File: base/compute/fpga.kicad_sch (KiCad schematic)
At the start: 17 parts, among them U4 W25X20CLSN, U5 ICE40UP5K-SG48ITR-FPGA_Lattice

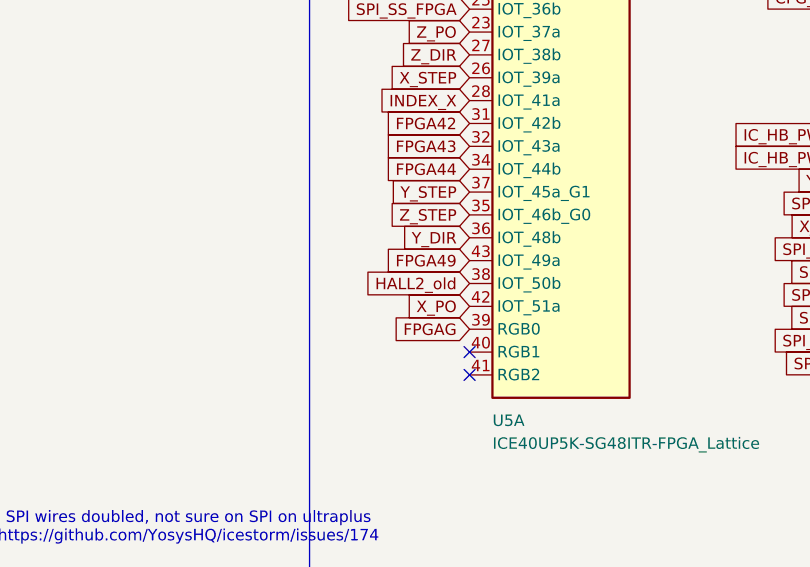
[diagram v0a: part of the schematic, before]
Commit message: kicost integration for compute and extension
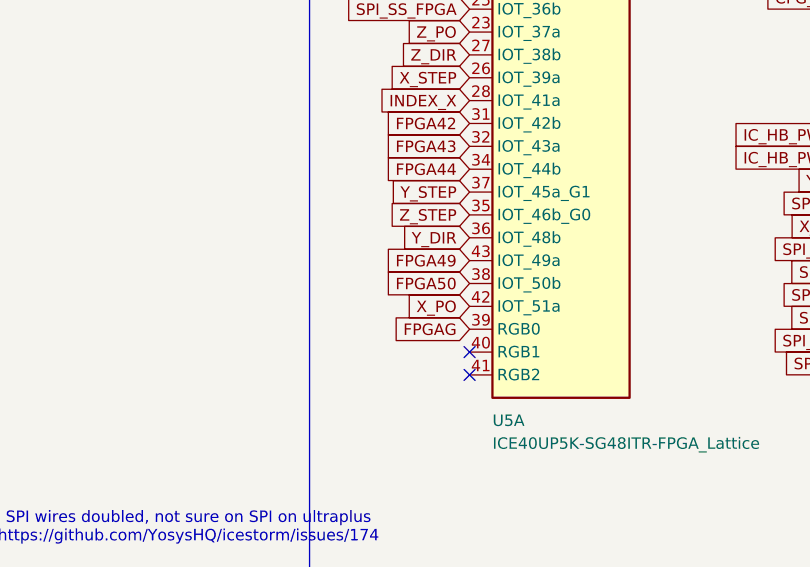
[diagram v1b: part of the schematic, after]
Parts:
- C12, C14, C3, C5, C6: Farnell 1414663 -> (none); Mouser 80-C0805C104J5R -> (none); Producer C0805C104J5RACTU -> (none); farnell# (none) -> 1414663; manf# (none) -> C0805C104J5RACTU; mouser# (none) -> 80-C0805C104J5R
- C13, C4, C7, C8: Farnell 2611942 -> (none); Mouser 81-GRM21BR61H475KE1L -> (none); Producer GRM21BR61H475KE51L -> (none); farnell# (none) -> 2611942; manf# (none) -> GRM21BR61H475KE51L; mouser# (none) -> 81-GRM21BR61H475KE1L
- D1: Farnell 1843668 -> (none); Mouser 621-B340A-F -> (none); Producer B340A-13-F -> (none); farnell# (none) -> 2393466; manf# (none) -> SD103AWS-E3-08; mouser# (none) -> 78-SD103AWS-HE3-18
- R1, R2, R3, R7: Farnell 2826162 -> (none); Mouser 71-CRCW080510K0JNEAC -> (none); Producer CRCW080510K0JNEAC -> (none); farnell# (none) -> 2826162; manf# (none) -> CRCW080510K0JNEAC; mouser# (none) -> 71-CRCW080510K0JNEAC
- R10: Farnell 1652906 -> (none); Mouser 71-CRCW0805-100 -> (none); Producer CRCW0805100RFKTA -> (none); farnell# (none) -> 1652906; manf# (none) -> CRCW0805100RFKTA; mouser# (none) -> 71-CRCW0805-100
- U4: Mouser 454-W25X20CLSNIG -> (none); Producer W25X20CLSNIG -> (none); manf# (none) -> W25X20CLSNIG; mouser# (none) -> 454-W25X20CLSNIG
- U5: Mouser 842-ICE40UP5K-SG48I -> (none); Producer ICE40UP5K-SG48I -> (none); manf# (none) -> ICE40UP5K-SG48I; mouser# (none) -> 842-ICE40UP5K-SG48I
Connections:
- net HALL2_old renamed FPGA50
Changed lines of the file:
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@@
 	(title_block
 		(title "Firestarter ")
-		(date "2024-07-25")
+		(date "2024-10-26")
 		(company "Hexastorm")
 		(comment 1 "v1")
@@
 		)
 	)
-	(global_label "HALL2_old"
+	(global_label "FPGA50"
 		(shape input)
 		(at 73.66 80.01 180)
@@
 			)
 		)
-		(property "Producer" "ICE40UP5K-SG48I"
+		(property "manf#" "ICE40UP5K-SG48I"
 			(at 199.39 58.42 0)
 			(effects
@@
 			)
 		)
-		(property "Mouser" "842-ICE40UP5K-SG48I"
+		(property "mouser#" "842-ICE40UP5K-SG48I"
 			(at 199.39 58.42 0)
 			(effects
@@
 			)
 		)
-		(property "Farnell" "2826162"
+		(property "farnell#" "2826162"
 			(at 158.75 57.15 0)
 			(effects
@@
 			)
 		)
-		(property "Producer" "CRCW080510K0JNEAC "
+		(property "manf#" "CRCW080510K0JNEAC"
 			(at 158.75 57.15 0)
 			(effects
@@
 			)
 		)
-		(property "Mouser" "71-CRCW080510K0JNEAC "
+		(property "mouser#" "71-CRCW080510K0JNEAC"
 			(at 158.75 57.15 0)
 			(effects
@@
 			)
 		)
-		(property "Farnell" "2826162"
+		(property "farnell#" "2826162"
 			(at 158.75 62.23 0)
 			(effects
@@
 			)
 		)
-		(property "Producer" "CRCW080510K0JNEAC "
+		(property "manf#" "CRCW080510K0JNEAC"
 			(at 158.75 62.23 0)
 			(effects
@@
 			)
 		)
-		(property "Mouser" "71-CRCW080510K0JNEAC "
+		(property "mouser#" "71-CRCW080510K0JNEAC"
 			(at 158.75 62.23 0)
 			(effects
@@
 			)
 		)
-		(property "Producer" "B340A-13-F"
+		(property "manf#" "SD103AWS-E3-08"
 			(at 175.26 109.22 0)
 			(effects
@@
 			)
 		)
-		(property "Farnell" "1843668 "
+		(property "farnell#" "2393466"
 			(at 175.26 109.22 0)
 			(effects
@@
 			)
 		)
-		(property "Mouser" "621-B340A-F"
+		(property "mouser#" "78-SD103AWS-HE3-18"
 			(at 175.26 109.22 0)
 			(effects
@@
 			)
 		)
-		(property "Producer" "ICE40UP5K-SG48I"
+		(property "manf#" "ICE40UP5K-SG48I"
 			(at 198.12 105.41 0)
 			(effects
@@
 			)
 		)
-		(property "Mouser" "842-ICE40UP5K-SG48I"
+		(property "mouser#" "842-ICE40UP5K-SG48I"
 			(at 198.12 105.41 0)
 			(effects
@@
 			)
 		)
-		(property "Mouser" "454-W25X20CLSNIG"
+		(property "mouser#" "454-W25X20CLSNIG"
 			(at 111.76 149.86 0)
 			(effects
@@
 			)
 		)
-		(property "Producer" "W25X20CLSNIG "
+		(property "manf#" "W25X20CLSNIG"
 			(at 111.76 149.86 0)
 			(effects
@@
 		)
 		(instances
-			(project ""
+			(project "main_board"
 				(path "/3f5fe6b7-98fc-4d3e-9567-f9f7202d1455/bdb11667-3ffd-4676-bd47-34e666a8a2df"
 					(reference "U4")
@@
 			)
 		)
-		(property "Producer" "C0805C104J5RACTU"
+		(property "manf#" "C0805C104J5RACTU"
 			(at 114.3 137.16 0)
 			(effects
@@
 			)
 		)
-		(property "Mouser" "80-C0805C104J5R "
+		(property "mouser#" "80-C0805C104J5R"
 			(at 114.3 137.16 0)
 			(effects
@@
 			)
 		)
-		(property "Farnell" "1414663 "
+		(property "farnell#" "1414663"
 			(at 114.3 137.16 0)
 			(effects
@@
 			)
 		)
-		(property "Producer" "C0805C104J5RACTU"
+		(property "manf#" "C0805C104J5RACTU"
 			(at 210.82 39.37 0)
 			(effects
@@
 			)
 		)
-		(property "Mouser" "80-C0805C104J5R "
+		(property "mouser#" "80-C0805C104J5R"
 			(at 210.82 39.37 0)
 			(effects
@@
 			)
 		)
-		(property "Farnell" "1414663 "
+		(property "farnell#" "1414663"
 			(at 210.82 39.37 0)
 			(effects
@@
 			)
 		)
-		(property "Producer" "GRM21BR61H475KE51L"
+		(property "manf#" "GRM21BR61H475KE51L"
 			(at 105.41 38.1 0)
 			(effects
@@
 			)
 		)
-		(property "Farnell" "2611942"
+		(property "farnell#" "2611942"
 			(at 105.41 38.1 0)
 			(effects
@@
 			)
 		)
-		(property "Mouser" "81-GRM21BR61H475KE1L"
+		(property "mouser#" "81-GRM21BR61H475KE1L"
 			(at 105.41 38.1 0)
 			(effects
@@
 			)
 		)
-		(property "Producer" "GRM21BR61H475KE51L"
+		(property "manf#" "GRM21BR61H475KE51L"
 			(at 151.13 36.83 0)
 			(effects
@@
 			)
 		)
-		(property "Farnell" "2611942"
+		(property "farnell#" "2611942"
 			(at 151.13 36.83 0)
 			(effects
@@
 			)
 		)
-		(property "Mouser" "81-GRM21BR61H475KE1L"
+		(property "mouser#" "81-GRM21BR61H475KE1L"
 			(at 151.13 36.83 0)
 			(effects
@@
 			)
 		)
-		(property "Producer" "ICE40UP5K-SG48I"
+		(property "manf#" "ICE40UP5K-SG48I"
 			(at 83.82 64.77 0)
 			(effects
@@
 			)
 		)
-		(property "Mouser" "842-ICE40UP5K-SG48I"
+		(property "mouser#" "842-ICE40UP5K-SG48I"
 			(at 83.82 64.77 0)
 			(effects
@@
 			)
 		)
-		(property "Producer" "GRM21BR61H475KE51L"
+		(property "manf#" "GRM21BR61H475KE51L"
 			(at 185.42 100.33 0)
 			(effects
@@
 			)
 		)
-		(property "Farnell" "2611942"
+		(property "farnell#" "2611942"
 			(at 185.42 100.33 0)
 			(effects
@@
 			)
 		)
-		(property "Mouser" "81-GRM21BR61H475KE1L"
+		(property "mouser#" "81-GRM21BR61H475KE1L"
 			(at 185.42 100.33 0)
 			(effects
@@
 			)
 		)
-		(property "Producer" "C0805C104J5RACTU"
+		(property "manf#" "C0805C104J5RACTU"
 			(at 95.25 38.1 0)
 			(effects
@@
 			)
 		)
-		(property "Mouser" "80-C0805C104J5R "
+		(property "mouser#" "80-C0805C104J5R"
 			(at 95.25 38.1 0)
 			(effects
@@
 			)
 		)
-		(property "Farnell" "1414663 "
+		(property "farnell#" "1414663"
 			(at 95.25 38.1 0)
 			(effects
@@
 			)
 		)
-		(property "Farnell" "2826162"
+		(property "farnell#" "2826162"
 			(at 82.55 138.43 0)
 			(effects
@@
 			)
 		)
-		(property "Producer" "CRCW080510K0JNEAC "
+		(property "manf#" "CRCW080510K0JNEAC"
 			(at 82.55 138.43 0)
 			(effects
@@
 			)
 		)
-		(property "Mouser" "71-CRCW080510K0JNEAC "
+		(property "mouser#" "71-CRCW080510K0JNEAC"
 			(at 82.55 138.43 0)
 			(effects
@@
 			)
 		)
-		(property "Producer" "C0805C104J5RACTU"
+		(property "manf#" "C0805C104J5RACTU"
 			(at 143.51 36.83 0)
 			(effects
@@
 			)
 		)
-		(property "Mouser" "80-C0805C104J5R "
+		(property "mouser#" "80-C0805C104J5R"
 			(at 143.51 36.83 0)
 			(effects
@@
 			)
 		)
-		(property "Farnell" "1414663 "
+		(property "farnell#" "1414663"
 			(at 143.51 36.83 0)
 			(effects
@@
 			)
 		)
-		(property "Producer" "GRM21BR61H475KE51L"
+		(property "manf#" "GRM21BR61H475KE51L"
 			(at 217.17 39.37 0)
 			(effects
@@
 			)
 		)
-		(property "Farnell" "2611942"
+		(property "farnell#" "2611942"
 			(at 217.17 39.37 0)
 			(effects
@@
 			)
 		)
-		(property "Mouser" "81-GRM21BR61H475KE1L"
+		(property "mouser#" "81-GRM21BR61H475KE1L"
 			(at 217.17 39.37 0)
 			(effects
@@
 			)
 		)
-		(property "Producer" "CRCW0805100RFKTA"
+		(property "manf#" "CRCW0805100RFKTA"
 			(at 175.26 102.87 90)
 			(effects
@@
 			)
 		)
-		(property "Mouser" "71-CRCW0805-100"
+		(property "mouser#" "71-CRCW0805-100"
 			(at 175.26 102.87 90)
 			(effects
@@
 			)
 		)
-		(property "Farnell" "1652906"
+		(property "farnell#" "1652906"
 			(at 175.26 102.87 90)
 			(effects
@@
 			)
 		)
-		(property "Producer" "C0805C104J5RACTU"
+		(property "manf#" "C0805C104J5RACTU"
 			(at 179.07 100.33 0)
 			(effects
@@
 			)
 		)
-		(property "Mouser" "80-C0805C104J5R "
+		(property "mouser#" "80-C0805C104J5R"
 			(at 179.07 100.33 0)
 			(effects
@@
 			)
 		)
-		(property "Farnell" "1414663 "
+		(property "farnell#" "1414663"
 			(at 179.07 100.33 0)
 			(effects
@@
 			)
 		)
-		(property "Producer" "ICE40UP5K-SG48I"
+		(property "manf#" "ICE40UP5K-SG48I"
 			(at 129.54 66.04 0)
 			(effects
@@
 			)
 		)
-		(property "Mouser" "842-ICE40UP5K-SG48I"
+		(property "mouser#" "842-ICE40UP5K-SG48I"
 			(at 129.54 66.04 0)
 			(effects
@@
 			)
 		)
-		(property "Farnell" "2826162"
+		(property "farnell#" "2826162"
 			(at 78.74 138.43 0)
 			(effects
@@
 			)
 		)
-		(property "Producer" "CRCW080510K0JNEAC "
+		(property "manf#" "CRCW080510K0JNEAC"
 			(at 78.74 138.43 0)
 			(effects
@@
 			)
 		)
-		(property "Mouser" "71-CRCW080510K0JNEAC "
+		(property "mouser#" "71-CRCW080510K0JNEAC"
 			(at 78.74 138.43 0)
 			(effects

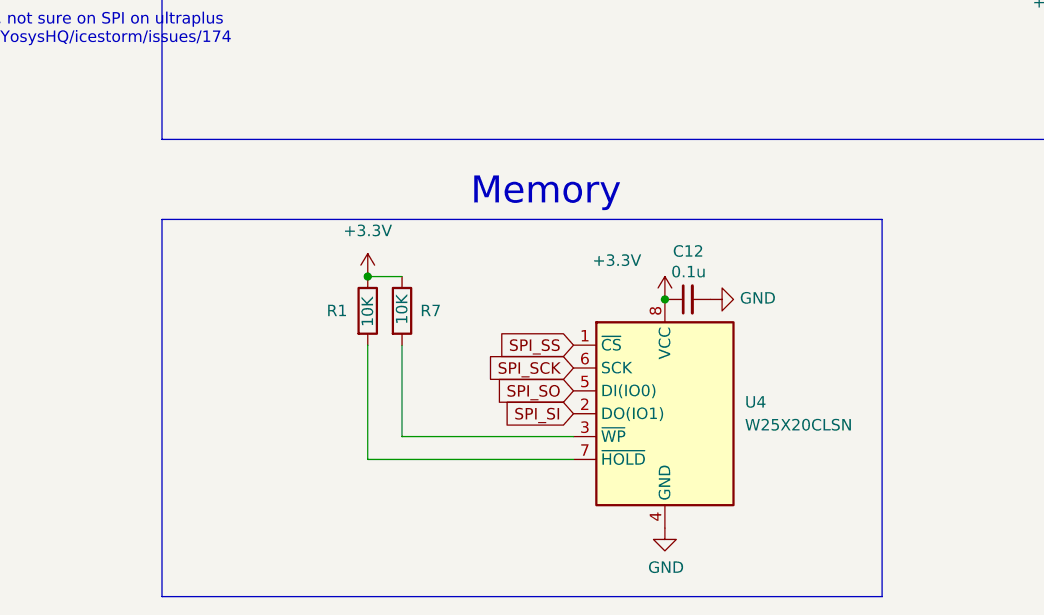
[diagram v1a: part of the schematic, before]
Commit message: fixed typo, added standoff lasermodule
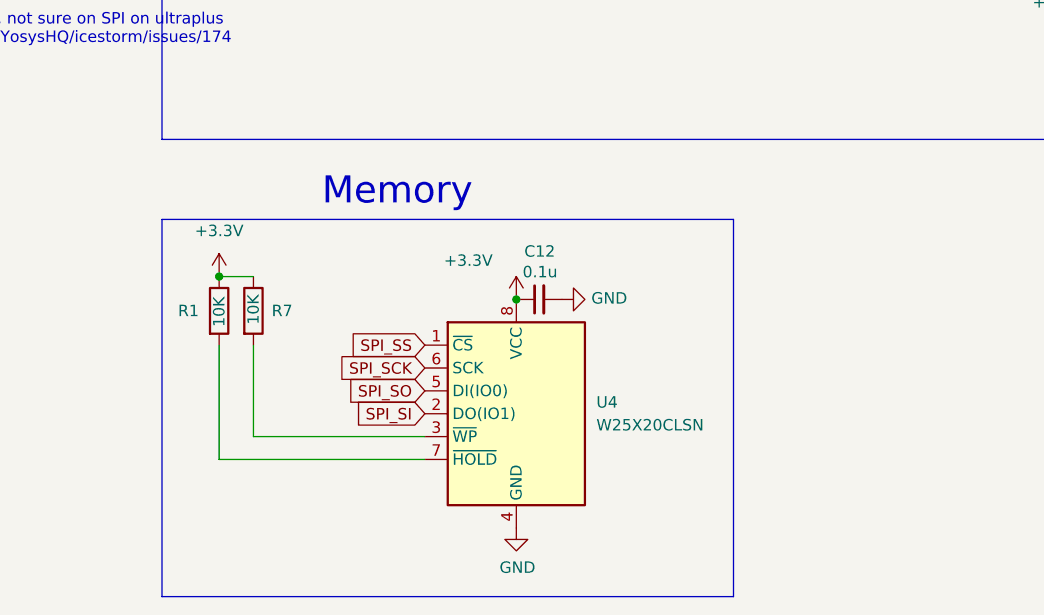
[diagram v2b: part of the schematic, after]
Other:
- moved on the sheet: C12, R1, R7, U4

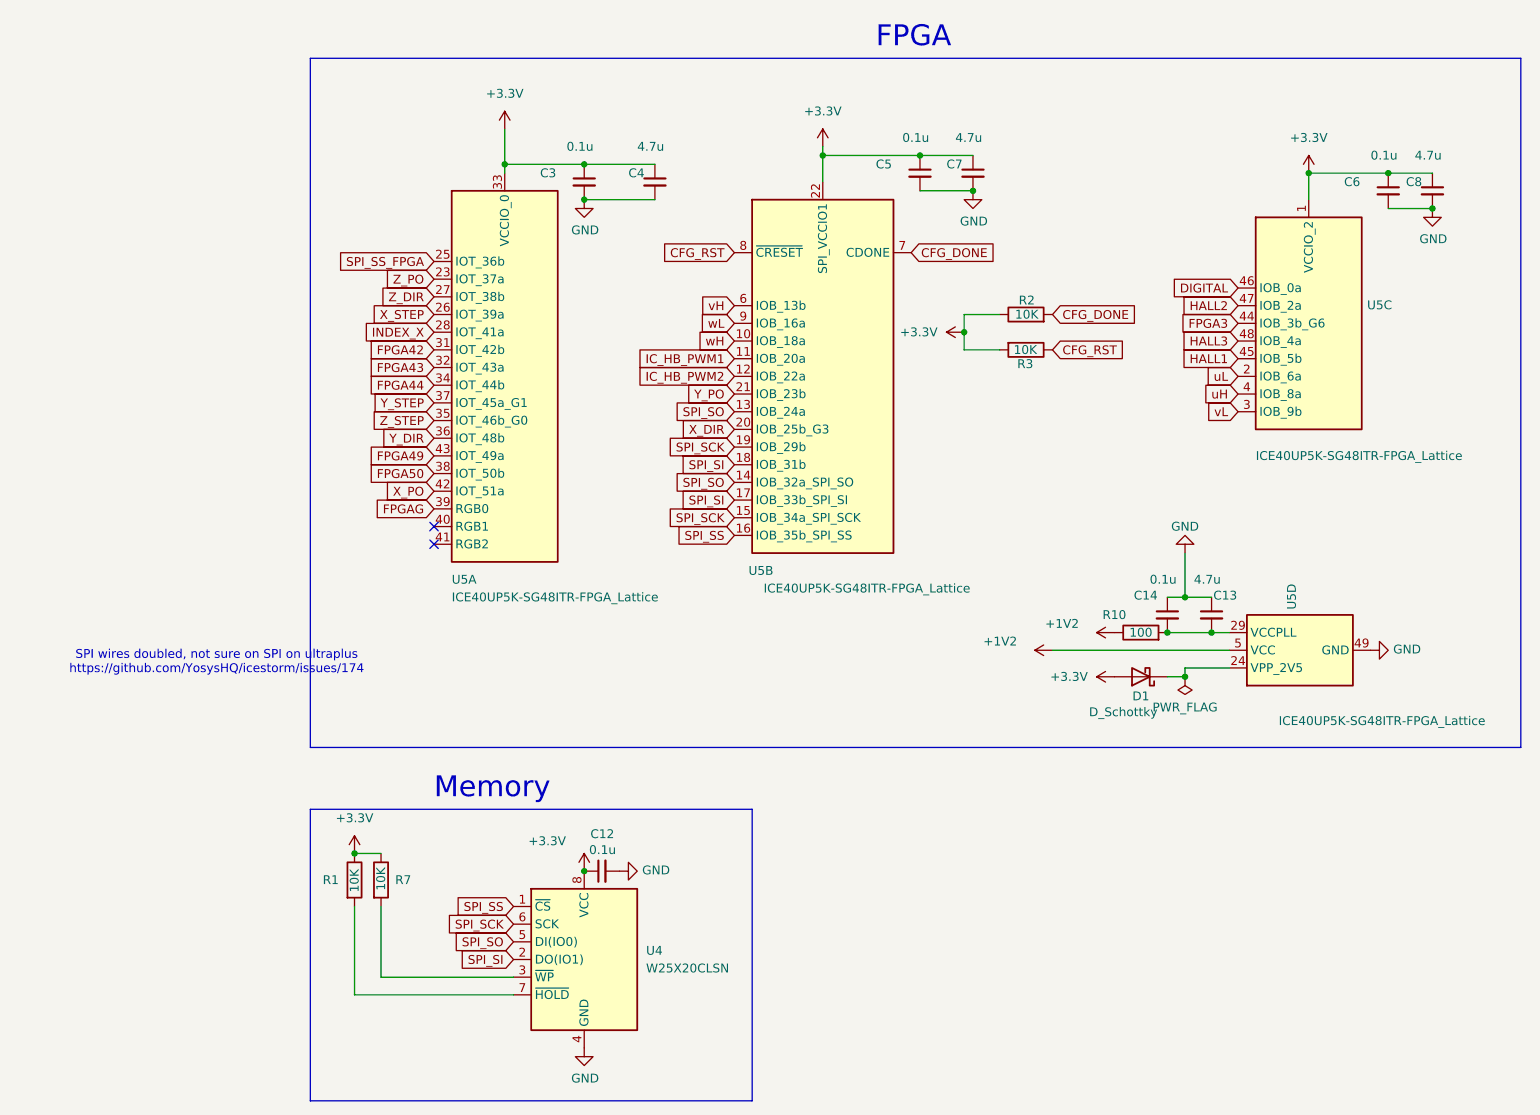
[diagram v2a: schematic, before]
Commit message: added mount felixprinter, standoffs
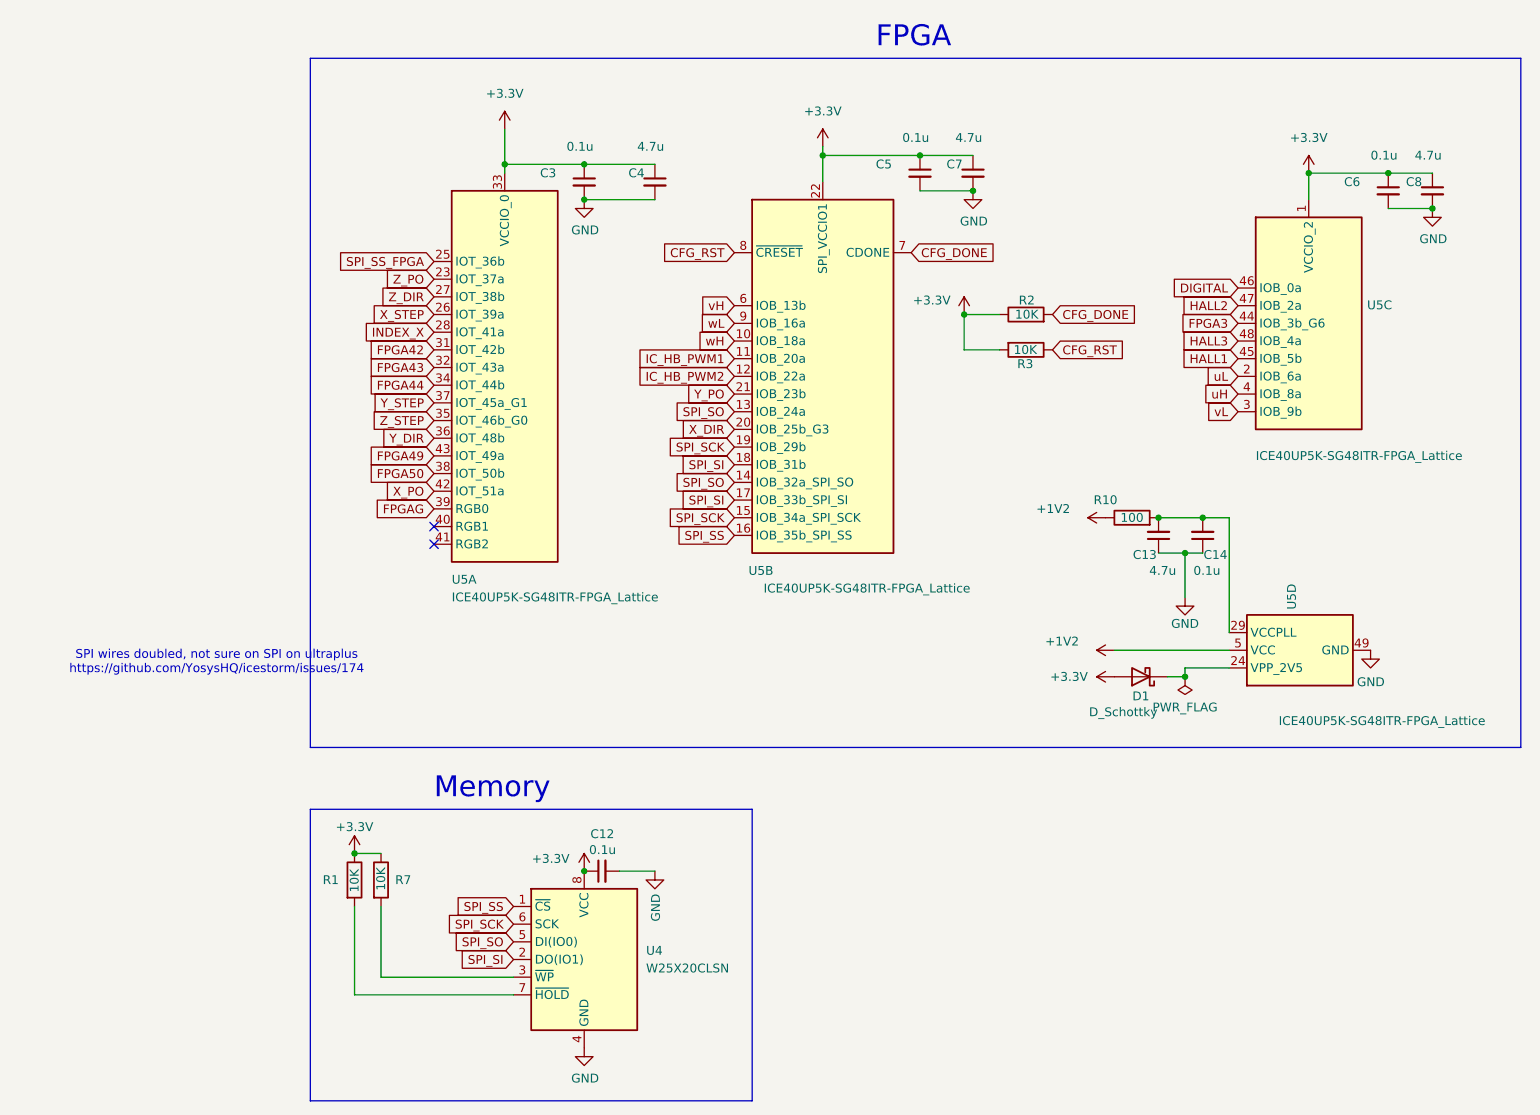
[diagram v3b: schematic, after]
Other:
- moved on the sheet: C13, C14, R10
